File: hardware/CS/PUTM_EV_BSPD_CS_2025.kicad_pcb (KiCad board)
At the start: 2 copper layers, 60 x 40 mm, 4 parts

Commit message: initial layout for Current Sensor
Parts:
- added 24V/500mA1: 500mA, Fuse:Fuse_1812_4532Metric, B.Cu at (104.2, 105.2)
- added C1: 1u, Capacitor_SMD:C_0805_2012Metric, B.Cu at (107.5, 101.1)
- added C2: 1u, Capacitor_SMD:C_0805_2012Metric, B.Cu at (114.2, 101.0)
- added C3: 1u, Capacitor_SMD:C_0805_2012Metric, B.Cu at (111.8, 101.1)
- added C4: 100nF, Capacitor_SMD:C_0603_1608Metric, B.Cu at (109.8, 100.8)
- added C5: 1u, Capacitor_SMD:C_0805_2012Metric, B.Cu at (117.8, 104.2)
- added C6: 100nF, Capacitor_SMD:C_0603_1608Metric, B.Cu at (118.0, 106.2)
- added C7: 100n, Capacitor_SMD:C_0603_1608Metric, B.Cu at (128.8, 98.2)
- added D1: LBD52A24L01, Diode_SMD:D_SOD-523, B.Cu at (103.5, 101.0)
- added D2: D, Diode_SMD:D_0603_1608Metric, B.Cu at (139.0, 99.8)
- added D3: D, Diode_SMD:D_0603_1608Metric, B.Cu at (139.0, 102.0)
- added J2: LEM, Snapeda:current_sensor, B.Cu at (121.9, 68.8)
- added J3: Conn_01x04, Snapeda:HARWIN_M80-5100422, B.Cu at (121.0, 112.0)
- added R1: 2k, Resistor_SMD:R_0603_1608Metric, B.Cu at (127.0, 94.2)
- added R10: 1k, Resistor_SMD:R_0603_1608Metric, B.Cu at (139.0, 97.8)
- added R11: 1k, Resistor_SMD:R_0603_1608Metric, B.Cu at (139.0, 104.0)
- added R12: 1k, Resistor_SMD:R_0603_1608Metric, B.Cu at (118.4, 89.5)
- added R13: 1k, Resistor_SMD:R_0603_1608Metric, B.Cu at (118.4, 85.9)
- added R2: 2k, Resistor_SMD:R_0603_1608Metric, B.Cu at (127.0, 92.2)
- added R3: 30k, Resistor_SMD:R_0603_1608Metric, B.Cu at (130.5, 92.2)
- added R4: 2k, Resistor_SMD:R_0603_1608Metric, B.Cu at (133.8, 94.2)
- added R5: 30k, Resistor_SMD:R_0603_1608Metric, B.Cu at (130.5, 94.2)
- added R6: 4k, Resistor_SMD:R_0603_1608Metric, B.Cu at (128.8, 100.2)
- added R7: 1k, Resistor_SMD:R_0603_1608Metric, B.Cu at (128.8, 102.2)
- added R8: 1k, Resistor_SMD:R_0603_1608Metric, B.Cu at (139.0, 93.2)
- added R9: 4k, Resistor_SMD:R_0603_1608Metric, B.Cu at (139.0, 95.2)
- added U1: MC78M12CDTG, Package_TO_SOT_SMD:TO-252-3_TabPin2, B.Cu at (106.8, 95.5)
- added U2: LM1117IMP-5.0, Package_TO_SOT_SMD:SOT-223-3_TabPin2, B.Cu at (119.2, 98.5)
- added U3: TLV9354QPWRQ1, Snapeda:DYY0014A_TEX-M, B.Cu at (133.5, 99.4)
- REF** (x4): moved to B.Cu
- moved REF** 65.0 mm to (106.0, 112.0), turned to 180 degrees
- moved REF** 45.1 mm to (138.2, 112.0), turned to 180 degrees
- moved REF** 41.8 mm to (124.3, 122.7), turned to 180 degrees
- moved REF** 12.2 mm to (115.8, 122.0), turned to 180 degrees
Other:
- board size 60 x 40 mm -> 42 x 35 mm

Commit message: First version of layout
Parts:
- removed the REF** at (138.2, 112.0)
- removed the REF** at (124.3, 122.7)
- added G***: LOGO, Samacsys:PUTM_Logo_8mm, F.Cu at (132.5, 103.5)
- J2: moved to F.Cu
- moved REF** 25.3 mm to (139.0, 112.0)
- moved J2 11.2 mm to (122.0, 80.0), turned to 0 degrees
- moved D3 11.0 mm to (133.5, 111.5), turned to 90 degrees
- moved R11 10.6 mm to (131.5, 111.5), turned to -90 degrees
- moved R12 10.3 mm to (119.5, 99.7)
- moved R13 9.85 mm to (119.5, 95.7)
- moved C3 9.22 mm to (114.8, 92.4), turned to 0 degrees
- moved R8 8.42 mm to (137.3, 101.5)
- moved R9 8.42 mm to (137.3, 103.5)
- moved R10 7.93 mm to (137.3, 105.5)
- moved D2 7.93 mm to (137.3, 107.5), turned to 180 degrees
- moved U2 6.49 mm to (113.5, 101.5), turned to 0 degrees
- moved C4 6.46 mm to (114.8, 96.8), turned to 0 degrees
- moved C2 6.27 mm to (114.8, 94.8), turned to 0 degrees
- moved R1 5.77 mm to (127.5, 100.0)
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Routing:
- net +5V: track 0.00 -> 61.8 mm, vias 0 -> 2
- net Net-(D2-A): track 0.00 -> 24.1 mm, vias 0 -> 2
- net Net-(D1-A1): track 0.00 -> 20.3 mm
- net /LV Battery : track 0.00 -> 14.6 mm
- net /OUT: track 0.00 -> 13.9 mm
- net /LEM Vref: track 0.00 -> 10.1 mm
- net Net-(R10-Pad2): track 0.00 -> 9.94 mm
- net /LEM Out: track 0.00 -> 9.41 mm
- net Net-(U3C-+): track 0.00 -> 8.99 mm
- net Net-(U3A-+): track 0.00 -> 7.96 mm
- net Net-(U3B-+): track 0.00 -> 6.50 mm
- net Net-(R4-Pad1): track 0.00 -> 6.43 mm, vias 0 -> 2
- net Net-(U3A--): track 0.00 -> 5.75 mm
- net Net-(R11-Pad1): track 0.00 -> 5.07 mm
- net Net-(D2-K): track 0.00 -> 2.67 mm
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- added copper zone on B.Cu, net +12V
- added copper zone on B.Cu, net GND
- added copper zone on F.Cu, net GND
- added copper zone on In1.Cu, net GND
- added copper zone on In2.Cu, net GND
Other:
- board size 42 x 35 mm -> 42 x 57.1 mm
- copper layers 2 -> 4
- board text added: "Current Sensor"
- board text added: "v.1.0.0"
- board text removed: "Template"
- board text removed: "v${REVISION}"

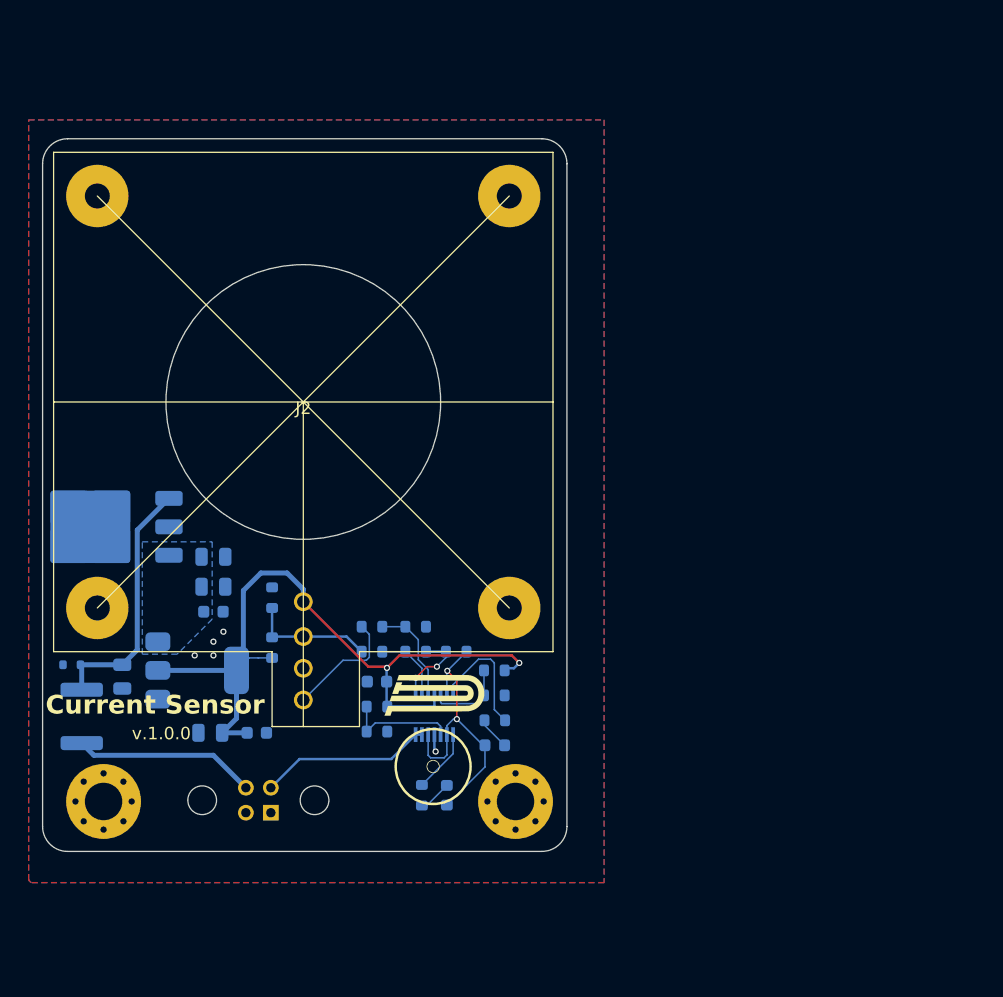
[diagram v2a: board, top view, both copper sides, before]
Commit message: Small changes in scheme and added vias
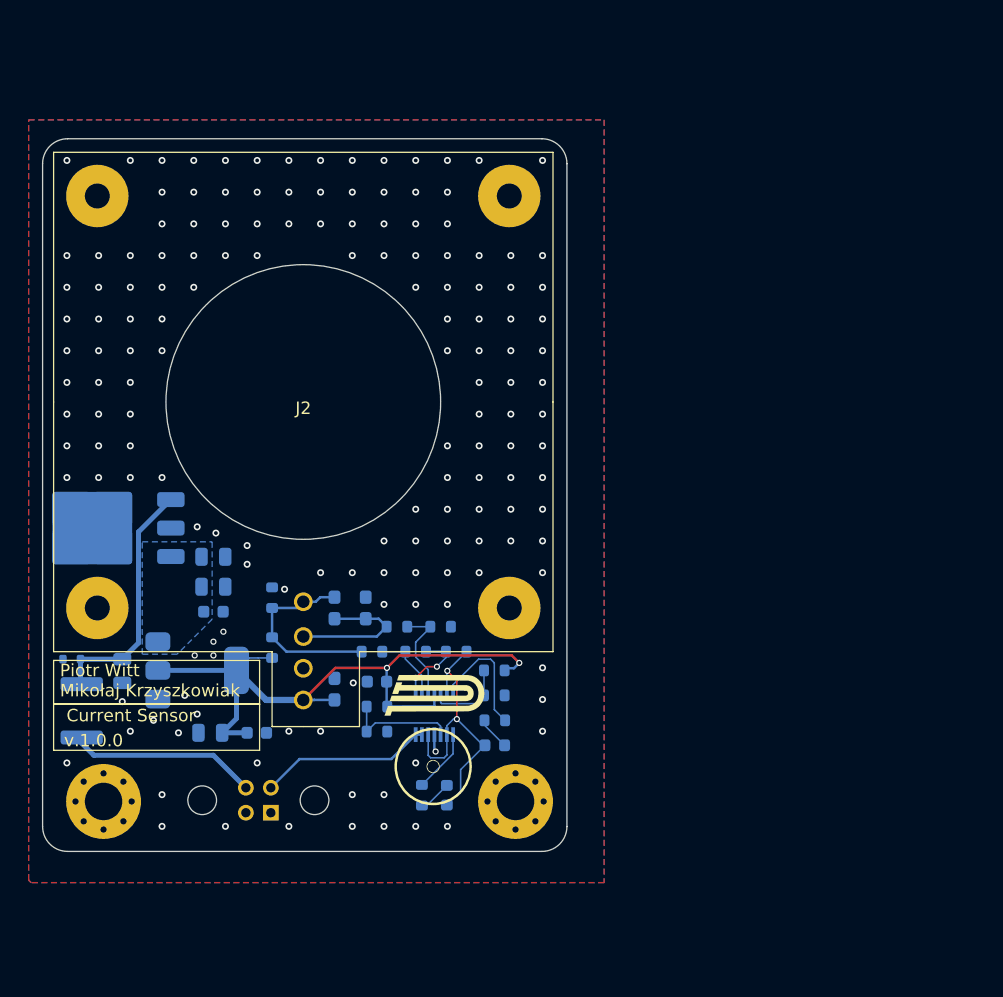
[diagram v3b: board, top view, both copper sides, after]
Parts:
- added C10: 47n, Capacitor_SMD:C_0603_1608Metric_Pad1.08x0.95mm_HandSolder, B.Cu at (124.5, 103.0)
- added C8: 47n, Capacitor_SMD:C_0603_1608Metric_Pad1.08x0.95mm_HandSolder, B.Cu at (124.5, 96.5)
- added C9: 4n7, Capacitor_SMD:C_0603_1608Metric_Pad1.08x0.95mm_HandSolder, B.Cu at (127.0, 96.5)
- moved R2 2.00 mm to (129.5, 98.0)
- moved R3 2.00 mm to (133.0, 98.0)
- moved 24V/500mA1 0.45 mm to (104.2, 104.7)
- moved C1 0.45 mm to (107.5, 101.5)
- moved D1 0.45 mm to (103.5, 100.6)
- moved U1 0.18 mm to (106.3, 90.1)
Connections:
- J2 pad 1: +5V -> /LEM Vref
- J2 pad 2: /LEM Vref -> /LEM Out
- J2 pad 4: /LEM Out -> +5V
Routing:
- net +5V: track 61.8 -> 56.1 mm
- net /LEM Vref: track 10.1 -> 15.4 mm
- net /LEM Out: track 9.41 -> 11.4 mm
- net GND: vias 5 -> 157
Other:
- board text added: "Piotr Witt Mikołaj Krzyszkowiak"

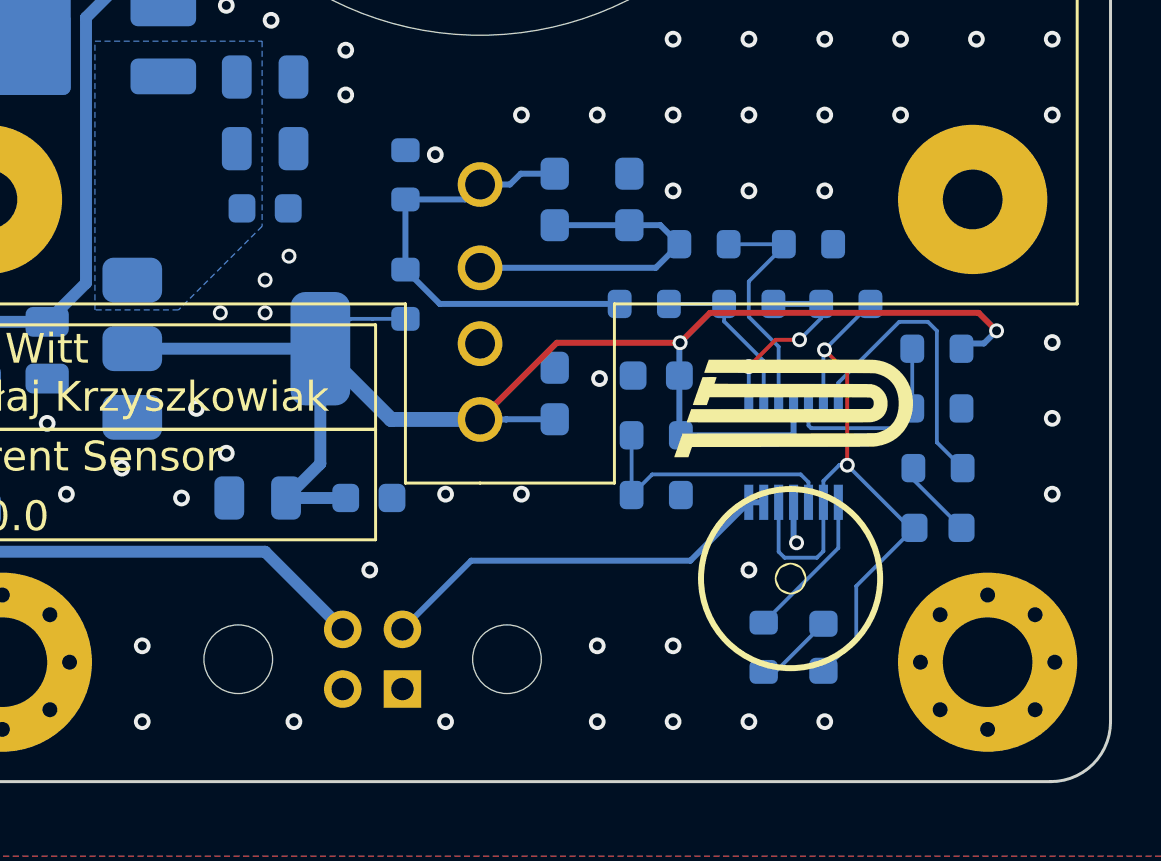
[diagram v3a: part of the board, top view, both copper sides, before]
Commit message: Added TVS Protection to output, change layout of omp amp
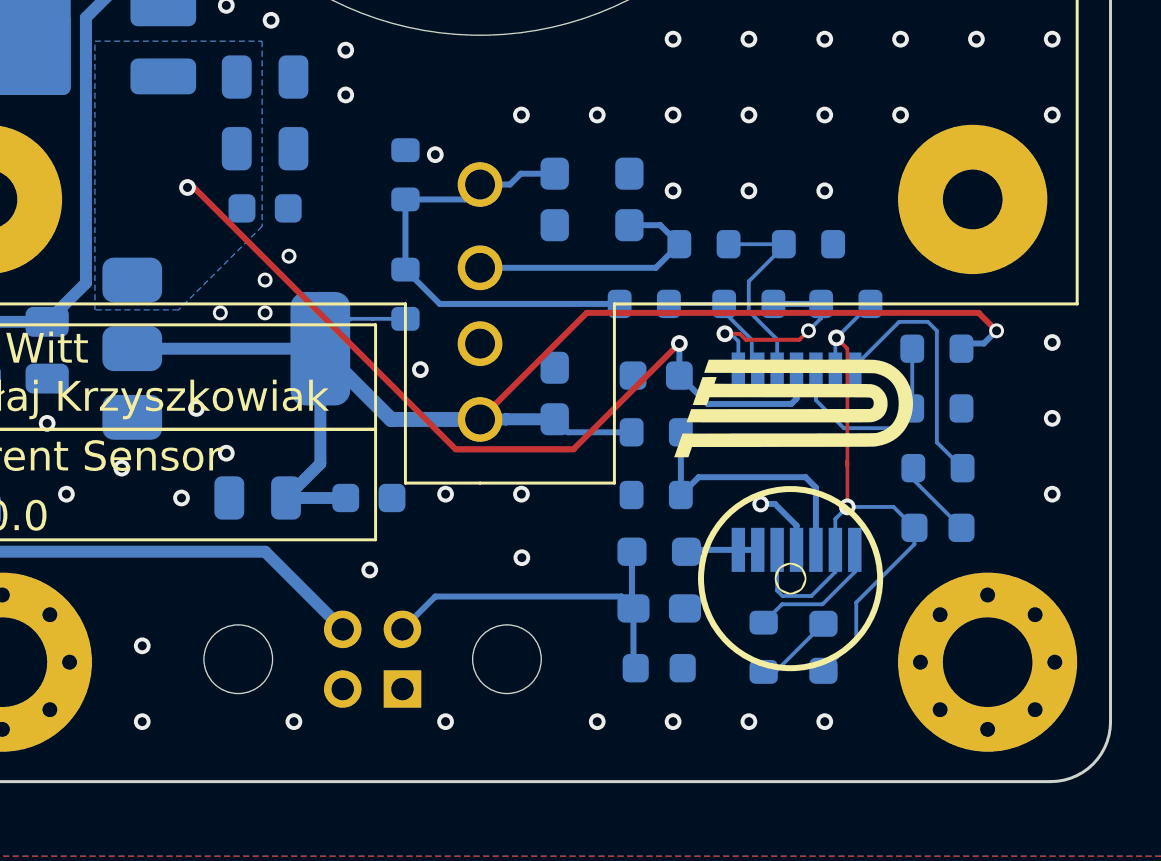
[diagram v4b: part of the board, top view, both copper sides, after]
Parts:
- added C11: 100n, Capacitor_SMD:C_0603_1608Metric_Pad1.08x0.95mm_HandSolder, B.Cu at (128.0, 110.2)
- added D4: TESDU5V0 RGG, Diode_SMD:D_0603_1608Metric, B.Cu at (128.0, 112.2)
- added R14: 800R, Resistor_SMD:R_0603_1608Metric_Pad0.98x0.95mm_HandSolder, B.Cu at (128.0, 108.3)
- D2, D3: value D -> SD0603S040S0R2
- U3: footprint Snapeda:DYY0014A_TEX-M -> Snapeda:SOP65P640X120-14N
- moved U3 0.32 mm to (132.6, 105.3)
- moved R6 0.10 mm to (127.9, 104.3), turned to 0 degrees
- turned R7 to 180 degrees
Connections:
- C7 pad 1: +5V -> +12V
- C8 pad 2: /LEM Out -> GND
- U3 pad 13: /OUT -> Net-(U3D--)
- U3 pad 14: /OUT -> Net-(U3D--)
- U3 pad 4: +5V -> +12V
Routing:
- net +12V: track 0.00 -> 27.9 mm, vias 0 -> 2
- net +5V: track 56.1 -> 50.7 mm, vias 2 -> 1
- net /LEM Out: track 11.4 -> 8.94 mm
- net Net-(U3D--): track 0.00 -> 2.41 mm
- net /OUT: track 13.9 -> 12.3 mm
- net Net-(R10-Pad2): track 9.94 -> 8.72 mm
- net Net-(U3A--): track 5.75 -> 4.68 mm
- net Net-(U3A-+): track 8.11 -> 7.09 mm
- net Net-(R4-Pad1): track 6.43 -> 7.35 mm
- net GND: track 1.40 -> 2.31 mm, vias 157 -> 155
- net Net-(R11-Pad1): track 5.07 -> 4.49 mm

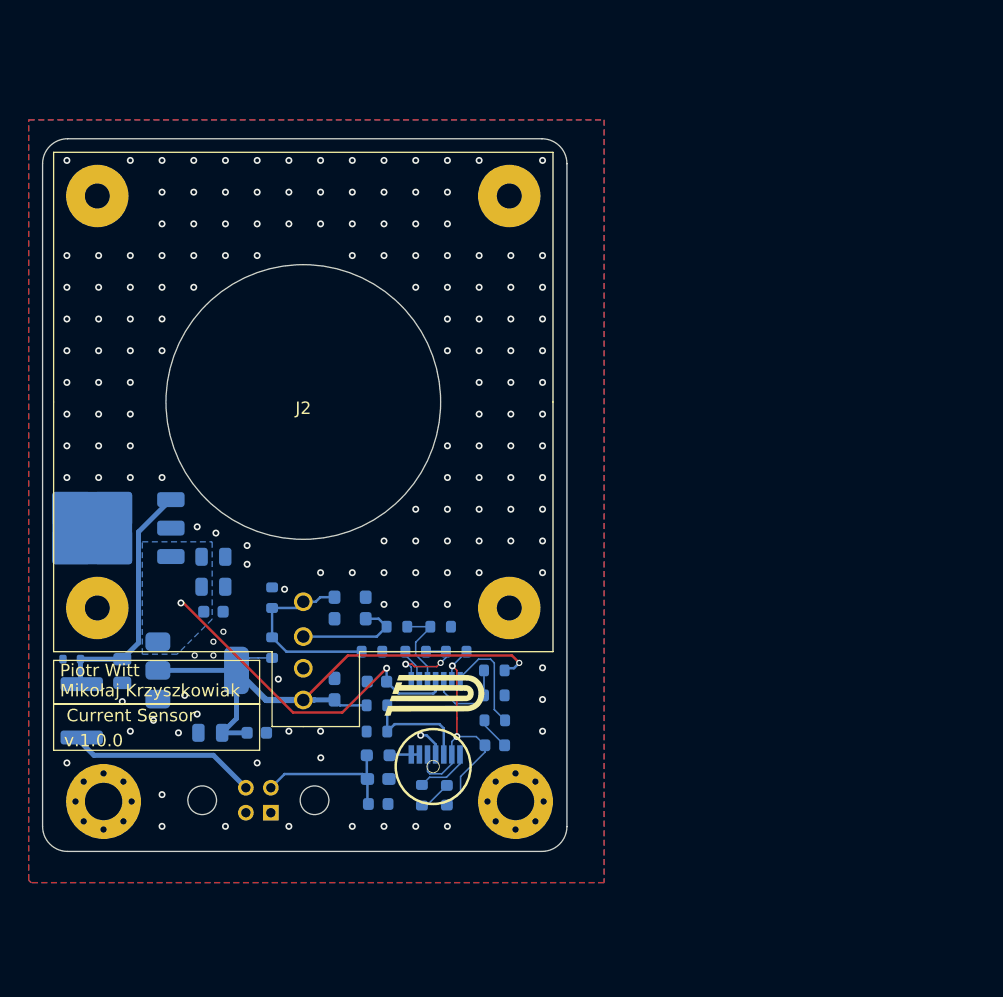
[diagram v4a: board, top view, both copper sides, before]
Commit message: Deleted GND loop around HV wire and changed output TVS layout
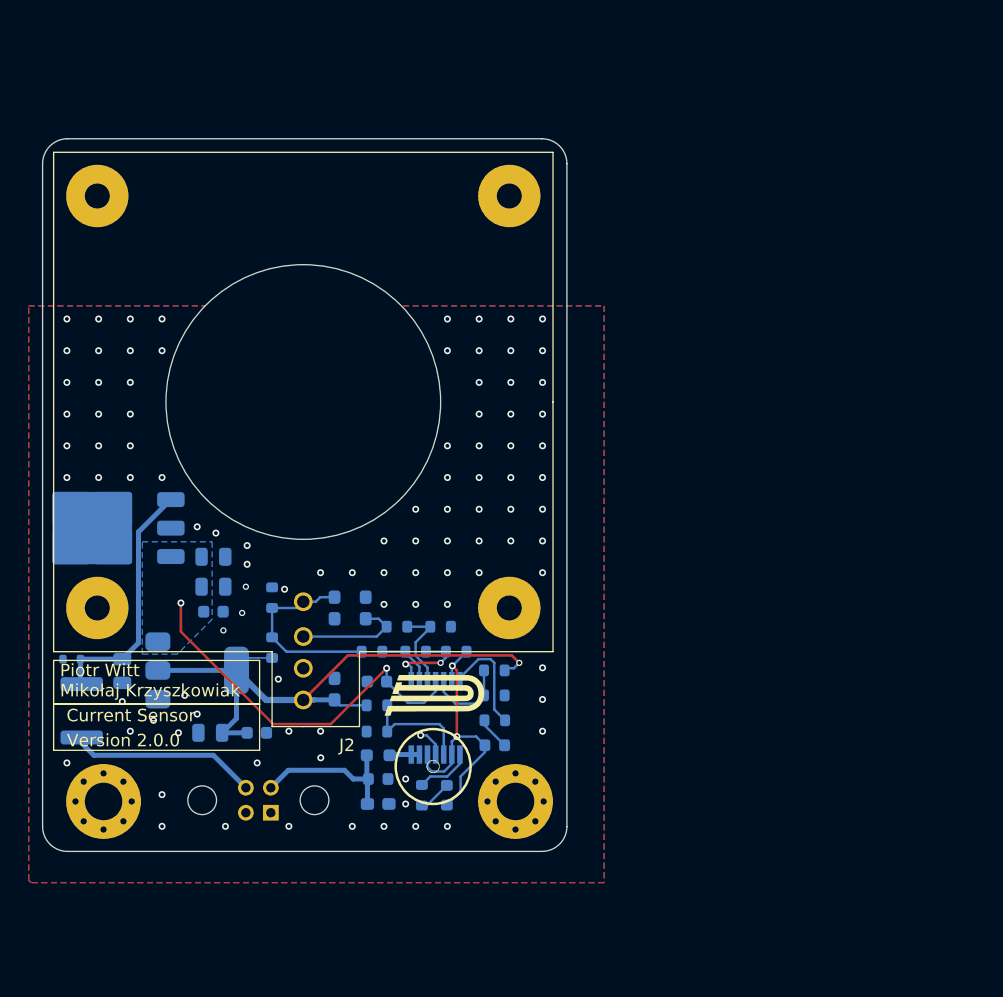
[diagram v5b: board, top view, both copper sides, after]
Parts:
- moved C11 2.00 mm to (128.0, 112.2)
- moved D4 2.00 mm to (128.0, 110.2)
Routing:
- net +12V: track 27.9 -> 30.6 mm
- net GND: vias 155 -> 98
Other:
- board text added: "Version 2.0.0"
- board text removed: "v.1.0.0"
